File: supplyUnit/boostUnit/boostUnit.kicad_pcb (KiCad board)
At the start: 2 copper layers, 79.4 x 31 mm, 26 parts, among them J1 Conn_02x03_Counter_Clockwise, J2 Conn_02x03_Counter_Clockwise

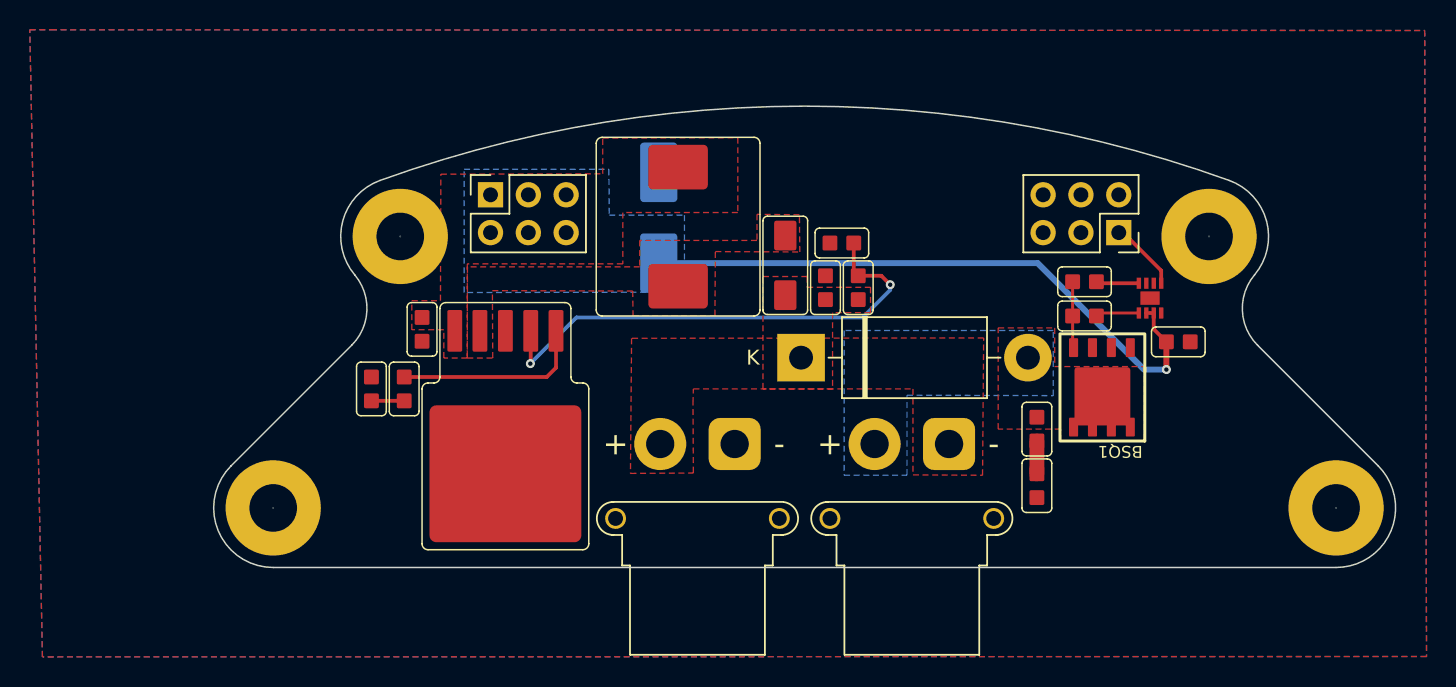
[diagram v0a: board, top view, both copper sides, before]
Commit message: boost placement
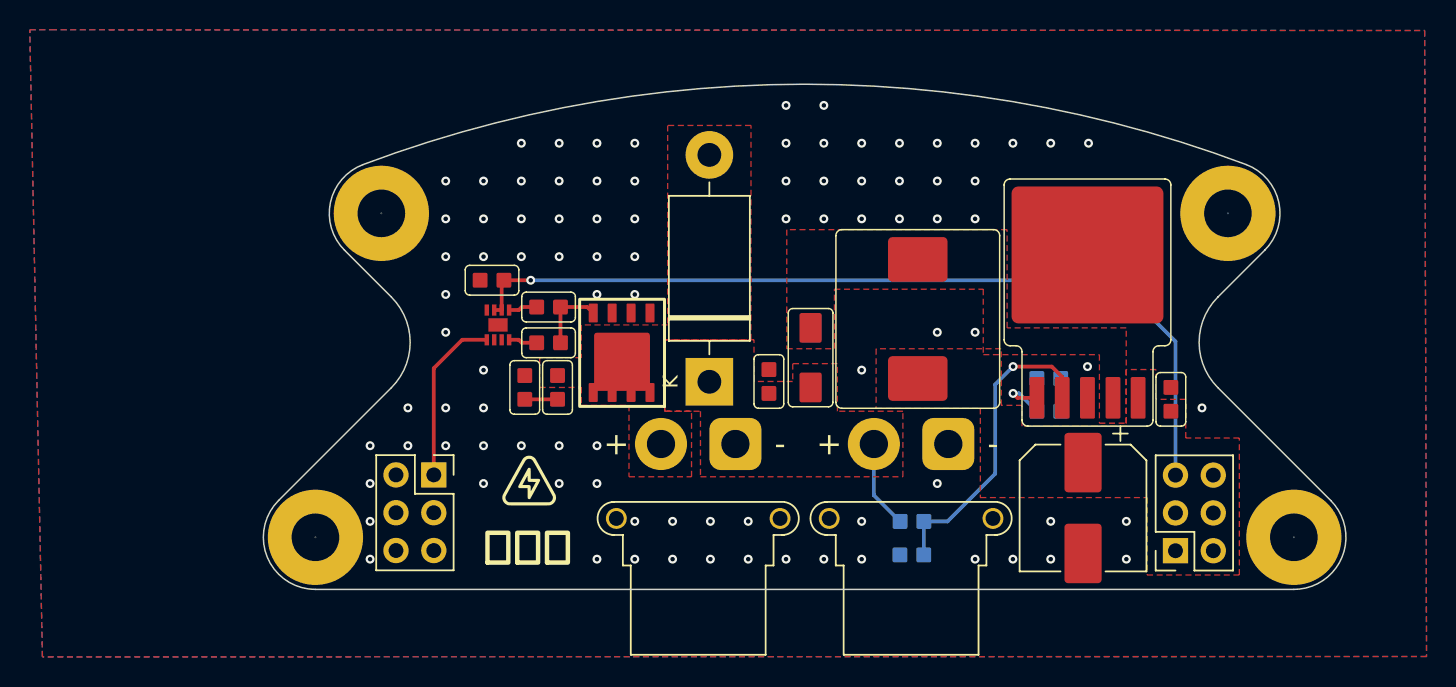
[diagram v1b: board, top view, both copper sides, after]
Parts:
- BC2: moved to F.Cu
- BC4, BR1, BR2, BR3: moved to B.Cu
- moved J1 51.9 mm to (162.1, 115.8), turned to 180 degrees
- moved BC1 50.5 mm to (161.8, 105.6), turned to 90 degrees
- moved J2 48.8 mm to (112.3, 110.7), turned to 0 degrees
- moved BSC1 46.3 mm to (116.2, 97.6), turned to 180 degrees
- moved BC4 45.5 mm to (153.6, 104.2), turned to 180 degrees
- moved BSU1 43.8 mm to (116.6, 100.6), turned to 90 degrees
- moved BR2 43.3 mm to (153.6, 106.4), turned to 0 degrees
- moved BIC1 39.1 mm to (156.2, 102.4), turned to 90 degrees
- moved BSR3 36.2 mm to (120.0, 101.8), turned to 0 degrees
- moved BSR2 36.0 mm to (120.0, 99.4), turned to 0 degrees
- moved BSC2 35.0 mm to (118.4, 104.8), turned to 90 degrees
- moved BC2 34.5 mm to (155.9, 112.9), turned to -90 degrees
- moved BSQ1 32.3 mm to (124.9, 102.5)
- moved BSR1 32.3 mm to (120.6, 104.8)
- moved BR3 21.5 mm to (144.4, 116.0)
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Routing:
- net +12V: track 41.7 -> 58.1 mm
- net Net-(BIC1-FDBK): track 33.6 -> 21.0 mm, vias 2 -> 1
- net Net-(BIC1-COMP): track 12.9 -> 3.82 mm, vias 0 -> 1
- net /Sol: track 4.76 -> 11.5 mm
- net +48V: track 0.00 -> 5.93 mm
- net Net-(BSU1-OUTH): track 2.93 -> 1.93 mm
- net Net-(BSU1-OUTL): track 2.89 -> 1.93 mm
- net GND: vias 0 -> 91
- removed copper zone on B.Cu, net +12V
- removed copper zone on B.Cu, net Net-(BSD1-A)
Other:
- board size 79.4 x 31 mm -> 72.7 x 33.9 mm
- rule pad_to_mask_clearance: 0.2 -> 0.15
- board text added: "雨子"
- board text added: "高電圧"

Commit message: 死
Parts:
- moved BR2 1.20 mm to (153.6, 105.2)
- moved BC4 1.20 mm to (153.6, 103.0)
- moved BC1 1.00 mm to (161.8, 104.6)
- moved BIC1 1.00 mm to (156.2, 101.4)
- moved BC2 0.70 mm to (155.9, 112.2)
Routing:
- net Net-(BIC1-FDBK): track 21.0 -> 21.6 mm
- net GND: vias 91 -> 1

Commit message: Boost Driver
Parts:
- BSU1: footprint Library:SON50P200X200X100-9N -> Package_SO:SOIC-8_3.9x4.9mm_P1.27mm
- moved BSC1 9.93 mm to (125.6, 94.4), turned to 90 degrees
- moved BSU1 6.88 mm to (120.6, 95.0), turned to 0 degrees
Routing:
- net +12V: track 58.1 -> 47.4 mm
- net /Sol: track 11.5 -> 21.8 mm
- net Net-(BSU1-OUTL): track 1.93 -> 6.53 mm
- net Net-(BSU1-OUTH): track 1.93 -> 6.09 mm
